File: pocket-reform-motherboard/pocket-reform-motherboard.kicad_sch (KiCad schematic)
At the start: 302 parts, among them J1 CHARGER, J10 1-2199230-6, J11 Conn_01x33, J12 2199230-5, J13 FH35C-31S-0.3HW(50), J14 USB_C_Receptacle, J15 CONN_SPK, J16 SAMTEC_TSM-106-02-X-SH-A, J17 Conn_01x03_Pin, J18 CONN_HEAD, J19 Conn_01x03_Pin, J2 DM3AT-SF-PEJM5, J20 QWIIC, J3 USB_C_Receptacle, J4 09452812561, J5 SYSCTL, J6 USB_INT1, J7 HDMI_D_1.4, J8 SIM_Card, J9 USB_C_Receptacle_USB2.0, SW1 SW_DIP_x01, SW2 RESET, U1 reform2-som-connector, U10 W25Q32JVSS, U11 PCF8523T, U12 AP22815, U13 TXS0108EPW, U14 SN74AVC1T45, U15 TPD4E02B04DQA, U16 TPD4E02B04DQA, U17 TPD12S521, U18 TLV320AIC3100, U19 TPD4E02B04DQA, U2 MAX1837EUT33+T, U20 TPD4E02B04DQA, U21 TPD4E02B04DQA, U22 TPD4E02B04DQA, U23 FUSB302BMPX, U24 TXS0108EPW, U3 LM2830XQMFE/NOPB, U4 TLV1117-18, U5 TPS5450DDAR, U6 TPS5450DDAR, U7 74LVC1G34, U8 RP2040, U9 TUSB8040PFP, Y1 24MHz, Y2 12MHz 18pF, Y3 32.768 kHz

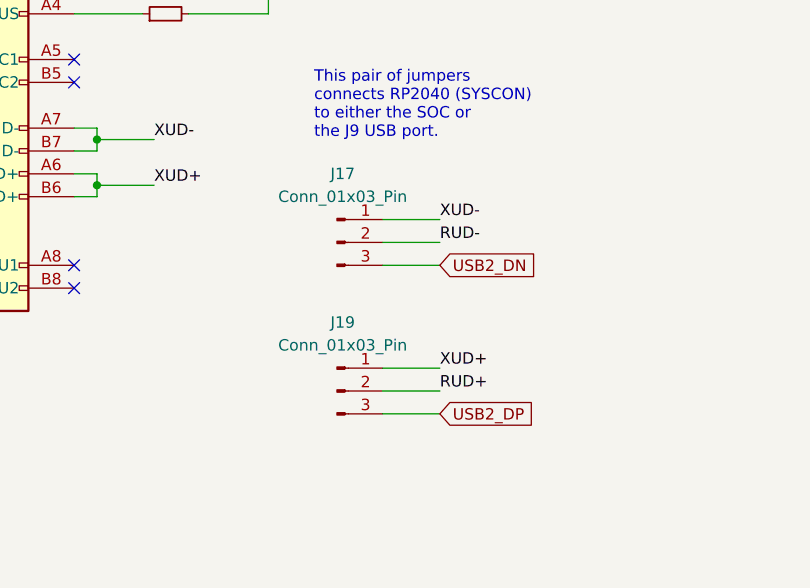
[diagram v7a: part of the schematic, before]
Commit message: D-2 fully routed
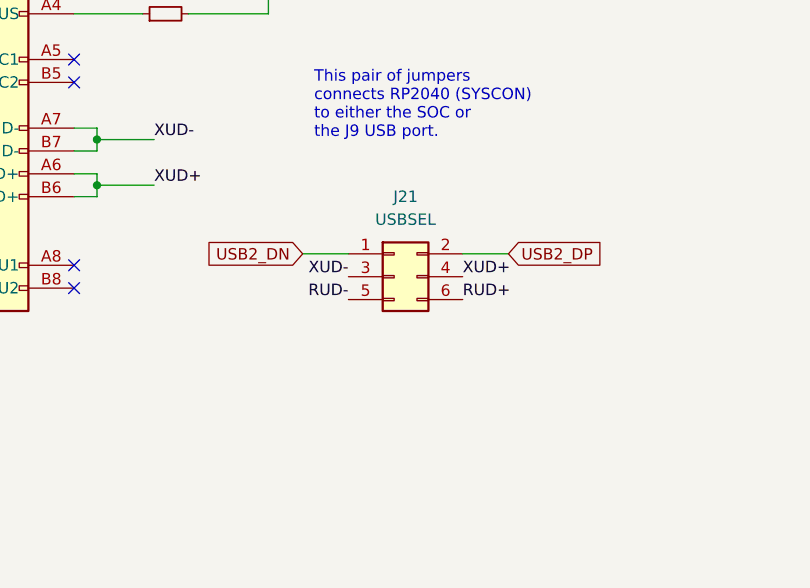
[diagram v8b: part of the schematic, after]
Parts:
- removed J17, J19: Conn_01x03_Pin, Connector_PinHeader_2.00mm:PinHeader_1x03_P2.00mm_Vertical_SMD_Pin1Left, symbol Connector:Conn_01x03_Pin
- added J21: USBSEL, Connector_PinHeader_2.00mm:PinHeader_2x03_P2.00mm_Vertical_SMD, symbol Connector_Generic:Conn_02x03_Odd_Even
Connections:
- net RUD+: now also J21.6 (Pin_6)
- net RUD-: now also J21.5 (Pin_5)
- net USB2_DN: now also J21.1 (Pin_1)
- net USB2_DP: now also J21.2 (Pin_2)
- net XUD+: now also J21.4 (Pin_4)
- net XUD-: now also J21.3 (Pin_3)
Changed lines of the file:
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@@
     (stroke (width 0) (type default))
   )
-  (wire (pts (xy 614.68 262.89) (xy 621.03 262.89))
-    (stroke (width 0) (type default))
-  )
   (wire (pts (xy 393.7 171.45) (xy 387.35 171.45))
     (stroke (width 0) (type default))
@@
     (stroke (width 0) (type default))
   )
-  (wire (pts (xy 614.68 251.46) (xy 621.03 251.46))
-    (stroke (width 0) (type default))
-  )
   (wire (pts (xy 1067.435 410.845) (xy 1068.705 410.845))
     (stroke (width 0) (type default))
@@
     (stroke (width 0) (type default))
   )
-  (wire (pts (xy 621.03 248.92) (xy 614.68 248.92))
-    (stroke (width 0) (type default))
-  )
   (wire (pts (xy 275.59 180.34) (xy 275.59 184.15))
     (stroke (width 0) (type default))
@@
     (stroke (width 0) (type default))
   )
-  (wire (pts (xy 614.68 246.38) (xy 621.03 246.38))
-    (stroke (width 0) (type default))
-  )
   (wire (pts (xy 849.63 441.96) (xy 853.44 441.96))
     (stroke (width 0) (type default))
@@
     (stroke (width 0) (type default))
   )
-  (wire (pts (xy 614.68 267.97) (xy 621.03 267.97))
-    (stroke (width 0) (type default))
-  )
   (wire (pts (xy 360.68 269.24) (xy 360.68 265.43))
     (stroke (width 0) (type default))
@@
     (stroke (width 0) (type default))
   )
+  (wire (pts (xy 610.87 250.19) (xy 605.79 250.19))
+    (stroke (width 0) (type default))
+  )
   (wire (pts (xy 760.73 204.47) (xy 783.59 204.47))
     (stroke (width 0) (type default))
@@
     (stroke (width 0) (type default))
   )
+  (wire (pts (xy 628.65 250.19) (xy 623.57 250.19))
+    (stroke (width 0) (type default))
+  )
   (wire (pts (xy 358.14 391.16) (xy 361.95 391.16))
     (stroke (width 0) (type default))
@@
     (stroke (width 0) (type default))
   )
-  (wire (pts (xy 621.03 265.43) (xy 614.68 265.43))
-    (stroke (width 0) (type default))
-  )
   (wire (pts (xy 406.4 163.83) (xy 406.4 162.56))
     (stroke (width 0) (type default))
@@
     (effects (font (size 1.27 1.27)) (justify right bottom))
   )
-  (label "XUD-" (at 621.03 246.38 0) (fields_autoplaced)
-    (effects (font (size 1.27 1.27)) (justify left bottom))
+  (label "XUD-" (at 610.87 252.73 180) (fields_autoplaced)
+    (effects (font (size 1.27 1.27)) (justify right bottom))
   )
   (label "USBH_1B_AC_TXP" (at 1011.6477 241.3 0) (fields_autoplaced)
@@
     (effects (font (size 1.27 1.27)) (justify left bottom))
   )
-  (label "XUD+" (at 621.03 262.89 0) (fields_autoplaced)
+  (label "XUD+" (at 623.57 252.73 0) (fields_autoplaced)
     (effects (font (size 1.27 1.27)) (justify left bottom))
   )
@@
     (effects (font (size 1.27 1.27)) (justify left bottom))
   )
-  (label "RUD+" (at 621.03 265.43 0) (fields_autoplaced)
-    (effects (font (size 1.27 1.27)) (justify left bottom))
-  )
   (label "~{M_WOWWAN}" (at 734.06 392.43 180) (fields_autoplaced)
     (effects (font (size 1.27 1.27)) (justify right bottom))
@@
     (effects (font (size 1.27 1.27)) (justify left bottom))
   )
+  (label "RUD+" (at 623.57 255.27 0) (fields_autoplaced)
+    (effects (font (size 1.27 1.27)) (justify left bottom))
+  )
   (label "M_CONFIG_2" (at 734.06 458.47 180) (fields_autoplaced)
     (effects (font (size 1.27 1.27)) (justify right bottom))
@@
     (effects (font (size 1.27 1.27)) (justify right bottom))
   )
-  (label "RUD-" (at 621.03 248.92 0) (fields_autoplaced)
-    (effects (font (size 1.27 1.27)) (justify left bottom))
-  )
   (label "M2_CLKREQn" (at 756.92 603.25 0) (fields_autoplaced)
     (effects (font (size 1.27 1.27)) (justify left bottom))
   )
+  (label "RUD-" (at 610.87 255.27 180) (fields_autoplaced)
+    (effects (font (size 1.27 1.27)) (justify right bottom))
+  )
   (label "AUD_3V3" (at 967.74 678.18 180) (fields_autoplaced)
     (effects (font (size 1.27 1.27)) (justify right bottom))
@@
     )
   )
-  (global_label "USB2_DN" (shape input) (at 621.03 251.46 0) (fields_autoplaced)
-    (effects (font (size 1.27 1.27)) (justify left))
-    (property "Intersheetrefs" "${INTERSHEET_REFS}" (at 52.07 -33.02 0)
+  (global_label "USB2_DN" (shape input) (at 605.79 250.19 180) (fields_autoplaced)
+    (effects (font (size 1.27 1.27)) (justify right))
+    (property "Intersheetrefs" "${INTERSHEET_REFS}" (at 1174.75 -34.29 0)
       (effects (font (size 1.27 1.27)) hide)
     )
@@
     )
   )
-  (global_label "USB2_DP" (shape input) (at 621.03 267.97 0) (fields_autoplaced)
-    (effects (font (size 1.27 1.27)) (justify left))
-    (property "Intersheetrefs" "${INTERSHEET_REFS}" (at 52.07 -21.59 0)
-      (effects (font (size 1.27 1.27)) hide)
-    )
-  )
   (global_label "DAC_SDA" (shape bidirectional) (at 139.7 514.35 180) (fields_autoplaced)
     (effects (font (size 1.27 1.27)) (justify right))
@@
     )
   )
+  (global_label "USB2_DP" (shape input) (at 628.65 250.19 0) (fields_autoplaced)
+    (effects (font (size 1.27 1.27)) (justify left))
+    (property "Intersheetrefs" "${INTERSHEET_REFS}" (at 639.5081 250.19 0)
+      (effects (font (size 1.27 1.27)) (justify left) hide)
+    )
+  )
   (global_label "USB2_RXN" (shape input) (at 195.58 525.78 180) (fields_autoplaced)
     (effects (font (size 1.27 1.27)) (justify right))
@@
     )
   )
-  (symbol (lib_id "Connector:Conn_01x03_Pin") (at 609.6 248.92 0) (unit 1)
-    (in_bom yes) (on_board yes) (dnp no) (fields_autoplaced)
-    (property "Reference" "J17" (at 610.235 241.3 0)
-      (effects (font (size 1.27 1.27)))
-    )
-    (property "Value" "Conn_01x03_Pin" (at 610.235 243.84 0)
-      (effects (font (size 1.27 1.27)))
-    )
-    (property "Footprint" "Connector_PinHeader_2.00mm:PinHeader_1x03_P2.00mm_Vertical_SMD_Pin1Left" (at 609.6 248.92 0)
-      (effects (font (size 1.27 1.27)) hide)
-    )
-    (property "Datasheet" "~" (at 609.6 248.92 0)
-      (effects (font (size 1.27 1.27)) hide)
-    )
-    (pin "1")
-    (pin "2")
-    (pin "3")
-    (instances
-      (project "pocket-reform-motherboard"
-        (path "/63c56ea4-91a3-4172-b9de-a4388cc8f894"
-          (reference "J17") (unit 1)
-        )
-      )
-    )
-  )
   (symbol (lib_id "Device:C_Small") (at 412.75 166.37 0) (mirror y) (unit 1)
     (in_bom yes) (on_board yes) (dnp no)
@@
     )
   )
+  (symbol (lib_id "Connector_Generic:Conn_02x03_Odd_Even") (at 615.95 252.73 0) (unit 1)
+    (in_bom yes) (on_board yes) (dnp no)
+    (property "Reference" "J21" (at 617.22 243.84 0)
+      (effects (font (size 1.27 1.27)))
+    )
+    (property "Value" "USBSEL" (at 617.22 246.38 0)
+      (effects (font (size 1.27 1.27)))
+    )
+    (property "Footprint" "Connector_PinHeader_2.00mm:PinHeader_2x03_P2.00mm_Vertical_SMD" (at 615.95 252.73 0)
+      (effects (font (size 1.27 1.27)) hide)
+    )
+    (property "Datasheet" "~" (at 615.95 252.73 0)
+      (effects (font (size 1.27 1.27)) hide)
+    )
+    (pin "1")
+    (pin "2")
+    (pin "3")
+    (pin "4")
+    (pin "5")
+    (pin "6")
+    (instances
+      (project "pocket-reform-motherboard"
+        (path "/63c56ea4-91a3-4172-b9de-a4388cc8f894"
+          (reference "J21") (unit 1)
+        )
+      )
+    )
+  )
   (symbol (lib_id "pocket-reform:TPD4E02B04DQA_RT") (at 1004.57 261.62 0) (unit 1)
     (in_bom yes) (on_board yes) (dnp no) (fields_autoplaced)
@@
     )
   )
-  (symbol (lib_id "Connector:Conn_01x03_Pin") (at 609.6 265.43 0) (unit 1)
-    (in_bom yes) (on_board yes) (dnp no) (fields_autoplaced)
-    (property "Reference" "J19" (at 610.235 257.81 0)
-      (effects (font (size 1.27 1.27)))
-    )
-    (property "Value" "Conn_01x03_Pin" (at 610.235 260.35 0)
-      (effects (font (size 1.27 1.27)))
-    )
-    (property "Footprint" "Connector_PinHeader_2.00mm:PinHeader_1x03_P2.00mm_Vertical_SMD_Pin1Left" (at 609.6 265.43 0)
-      (effects (font (size 1.27 1.27)) hide)
-    )
-    (property "Datasheet" "~" (at 609.6 265.43 0)
-      (effects (font (size 1.27 1.27)) hide)
-    )
-    (pin "1")
-    (pin "2")
-    (pin "3")
-    (instances
-      (project "pocket-reform-motherboard"
-        (path "/63c56ea4-91a3-4172-b9de-a4388cc8f894"
-          (reference "J19") (unit 1)
-        )
-      )
-    )
-  )
   (symbol (lib_id "power:GND") (at 269.24 544.83 0) (unit 1)
     (in_bom yes) (on_board yes) (dnp no)
@@
     (pin "30")
     (pin "31")
-    (pin "S1")
-    (pin "S2")
     (pin "4")
     (pin "5")
@@
     (pin "8")
     (pin "9")
+    (pin "S1")
+    (pin "S2")
     (instances
       (project "pocket-reform-motherboard"
